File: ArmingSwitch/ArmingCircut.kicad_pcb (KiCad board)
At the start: 2 copper layers, 7 parts, among them J1 Conn_01x02_Male, J2 Conn_01x02_Male, J3 Conn_01x02_Male

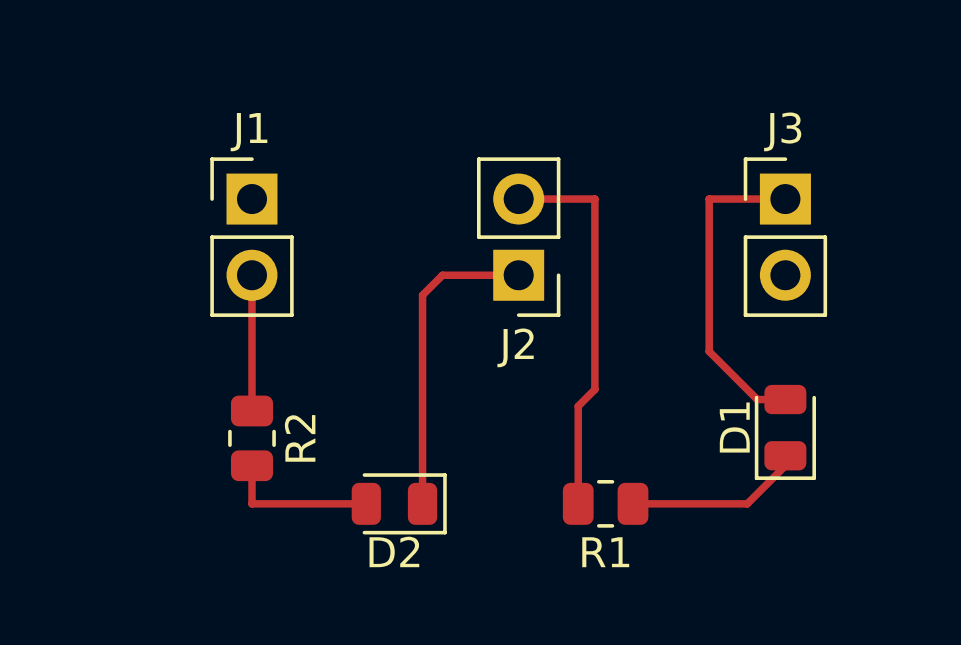
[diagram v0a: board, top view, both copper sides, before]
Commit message: moved components around
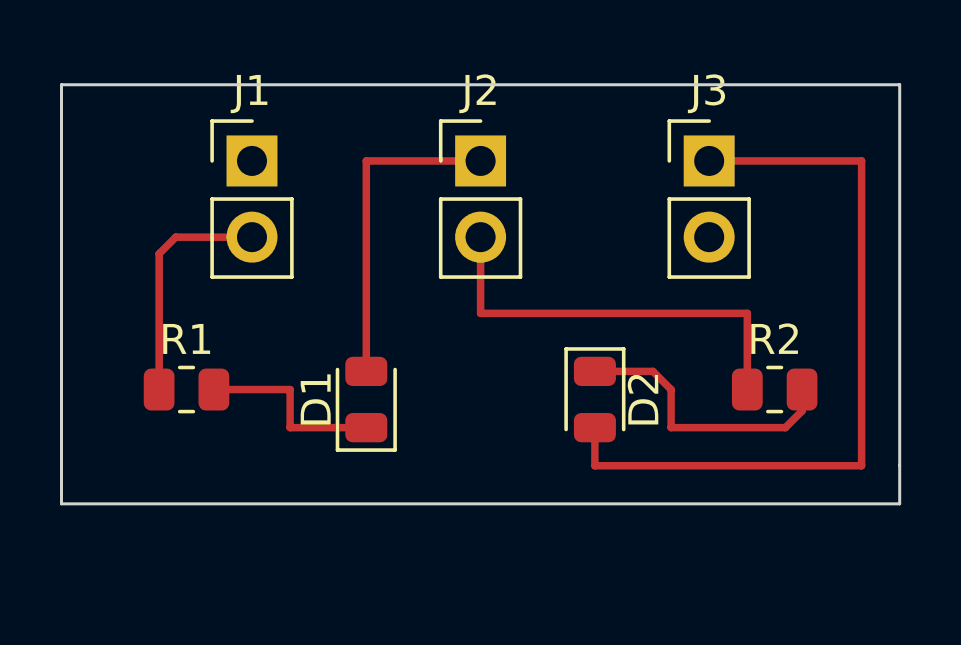
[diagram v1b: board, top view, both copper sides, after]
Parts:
- moved R2 17.5 mm to (157.1, 113.0), turned to 0 degrees
- moved R1 14.5 mm to (137.5, 113.0), turned to 0 degrees
- moved D1 14.0 mm to (143.5, 113.4)
- moved D2 7.53 mm to (151.1, 113.4), turned to 270 degrees
- moved J2 4.02 mm to (147.3, 105.4), turned to 0 degrees
- moved J3 2.84 mm to (154.9, 105.4)
- moved J1 1.27 mm to (139.7, 105.4)
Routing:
- net (no net): track 49.7 -> 73.8 mm
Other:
- board outline added: 27.9 x 14 mm

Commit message: traces look cooler, imo
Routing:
- net (no net): track 73.8 -> 65.6 mm

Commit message: added text
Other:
- board text added: "Arming Switch"

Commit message: text
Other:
- board size 27.9 x 14 mm -> 27.9 x 15.2 mm
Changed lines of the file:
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@@
   (general
     (thickness 1.6)
-    (drawings 6)
+    (drawings 8)
     (tracks 24)
     (zones 0)
@@
     )
   )
+  (gr_line (start 133.35 101.6) (end 133.35 102.87) (layer Edge.Cuts) (width 0.1))
+  (gr_line (start 161.29 101.6) (end 161.29 102.87) (layer Edge.Cuts) (width 0.1))
   (gr_text "Arming\nSwitch" (at 147.32 115.57) (layer F.Cu)
     (effects (font (size 0.75 0.75) (thickness 0.125)))
@@
   (gr_line (start 133.35 116.84) (end 161.29 116.84) (layer Edge.Cuts) (width 0.1))
   (gr_line (start 133.35 102.87) (end 133.35 116.84) (layer Edge.Cuts) (width 0.1))
-  (gr_line (start 161.29 102.87) (end 133.35 102.87) (layer Edge.Cuts) (width 0.1))
+  (gr_line (start 161.29 101.6) (end 133.35 101.6) (layer Edge.Cuts) (width 0.1))
   (gr_line (start 161.29 115.57) (end 161.29 102.87) (layer Edge.Cuts) (width 0.1))
   (segment (start 136.605 108.505) (end 137.16 107.95) (width 0.25) (layer F.Cu) (net 0))

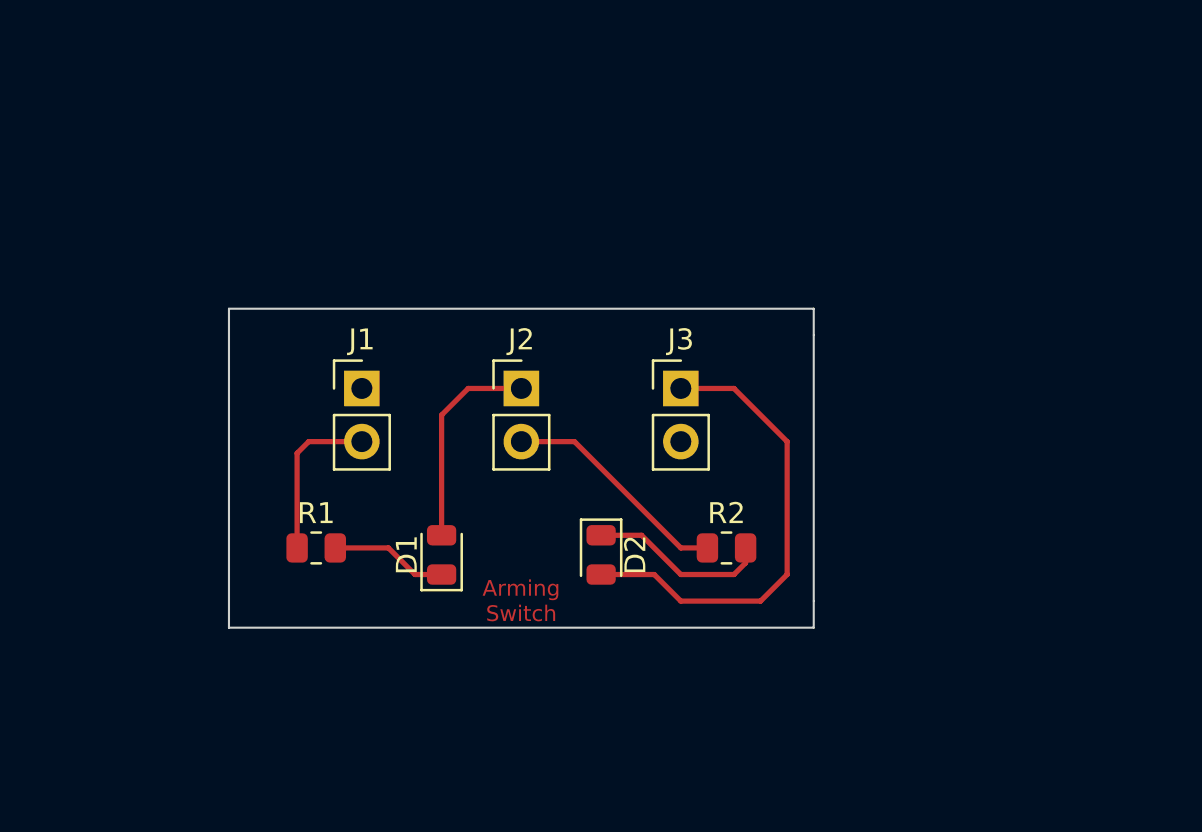
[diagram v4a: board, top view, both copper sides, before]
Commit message: added screw terminals
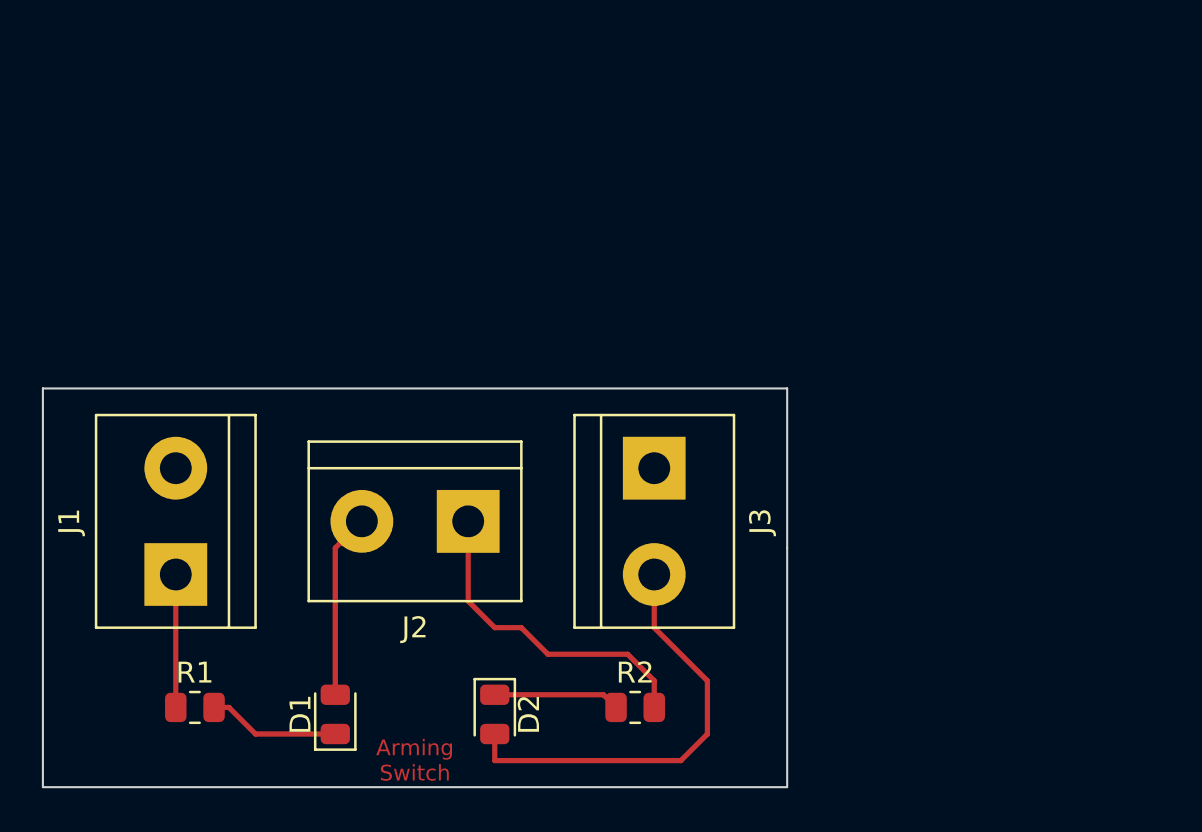
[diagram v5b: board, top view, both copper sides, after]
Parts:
- J1, J2, J3: value Conn_01x02_Male -> Screw_Terminal_01x02; footprint Connector_PinHeader_2.54mm:PinHeader_1x02_P2.54mm_Vertical -> TerminalBlock:TerminalBlock_bornier-2_P5.08mm
- moved J1 12.6 mm to (130.8, 114.3), turned to 90 degrees
- moved R1 9.57 mm to (131.7, 120.7)
- moved D1 9.16 mm to (138.4, 121.0)
- moved D2 9.16 mm to (146.1, 121.0)
- moved R2 8.78 mm to (152.8, 120.7)
- moved J2 6.84 mm to (144.8, 111.8), turned to 180 degrees
- moved J3 4.02 mm to (153.7, 109.2), turned to 270 degrees
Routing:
- net (no net): track 65.6 -> 63.7 mm
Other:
- board size 27.9 x 15.2 mm -> 35.6 x 19 mm

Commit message: no more errors!
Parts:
- moved R1 30.2 mm to (157.8, 105.4)
- moved D2 26.1 mm to (167.6, 106.3), turned to 90 degrees
- moved J1 23.4 mm to (146.1, 96.5), turned to 0 degrees
- moved D1 20.2 mm to (152.4, 106.3)
- moved J3 19.8 mm to (168.9, 96.5), turned to 0 degrees
- moved J2 19.8 mm to (157.5, 96.5), turned to 0 degrees
- moved R2 17.9 mm to (162.2, 105.4)
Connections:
- D1 pad 1: (no net) -> Net-(D1-Pad1)
- D1 pad 2: (no net) -> Net-(D1-Pad2)
- D2 pad 1: (no net) -> Net-(D2-Pad1)
- D2 pad 2: (no net) -> Net-(D2-Pad2)
- J1 pad 1: (no net) -> Net-(D1-Pad2)
- J1 pad 2: (no net) -> +5V
- J2 pad 1: (no net) -> Net-(D2-Pad2)
- J2 pad 2: (no net) -> Net-(D1-Pad2)
- J3 pad 1: (no net) -> Net-(D2-Pad2)
- J3 pad 2: (no net) -> /ArmingSwitch/ArmingSwitch
- R1 pad 1: (no net) -> Net-(D1-Pad1)
- R1 pad 2: (no net) -> GND
- R2 pad 1: (no net) -> GND
- R2 pad 2: (no net) -> Net-(D2-Pad1)
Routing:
- net (no net): track 63.7 -> 0.00 mm
- net Net-(D2-Pad2): track 0.00 -> 31.3 mm
- net Net-(D1-Pad2): track 0.00 -> 31.3 mm
- net Net-(D1-Pad1): track 0.00 -> 11.3 mm
- net Net-(D2-Pad1): track 0.00 -> 5.63 mm
- net GND: track 0.00 -> 2.54 mm
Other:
- board size 35.6 x 19 mm -> 35.6 x 20.3 mm
